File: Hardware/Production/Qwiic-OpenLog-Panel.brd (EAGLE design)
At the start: 90.4 x 94.2 mm, 261 parts, among them J1 SMD, J10 PTH, J11 SMD, J12 ISP, J13 SMD, J14 PTH, J15 SMD, J16 ISP, J17 SMD, J18 PTH, J19 SMD, J2 SMD, J20 ISP, J21 SMD, J22 PTH, J23 SMD, J24 ISP, J25 SMD, J26 PTH, J27 SMD, J28 ISP, J29 SMD, J3 PTH, J30 PTH, J31 SMD, J32 ISP, J33 SMD, J34 PTH, J35 SMD, J36 ISP, J4 SMD, J5 ISP, J6 PTH, J7 SMD, J8 ISP, J9 SMD, Q1 16MHZ, Q2 16MHZ, Q3 16MHZ, Q4 16MHZ, Q5 16MHZ, Q6 16MHZ, Q7 16MHZ, Q8 16MHZ, Q9 16MHZ, U1 microSD Socket, U10 ATMEGA328P_TQFP, U11 microSD Socket, U12 ATMEGA328P_TQFP, U13 microSD Socket, U14 ATMEGA328P_TQFP, U15 microSD Socket, U16 ATMEGA328P_TQFP, U17 microSD Socket, U18 ATMEGA328P_TQFP, U2 ATMEGA328P_TQFP, U3 microSD Socket, U4 ATMEGA328P_TQFP, U5 microSD Socket, U6 ATMEGA328P_TQFP, U7 microSD Socket, U8 ATMEGA328P_TQFP, U9 microSD Socket

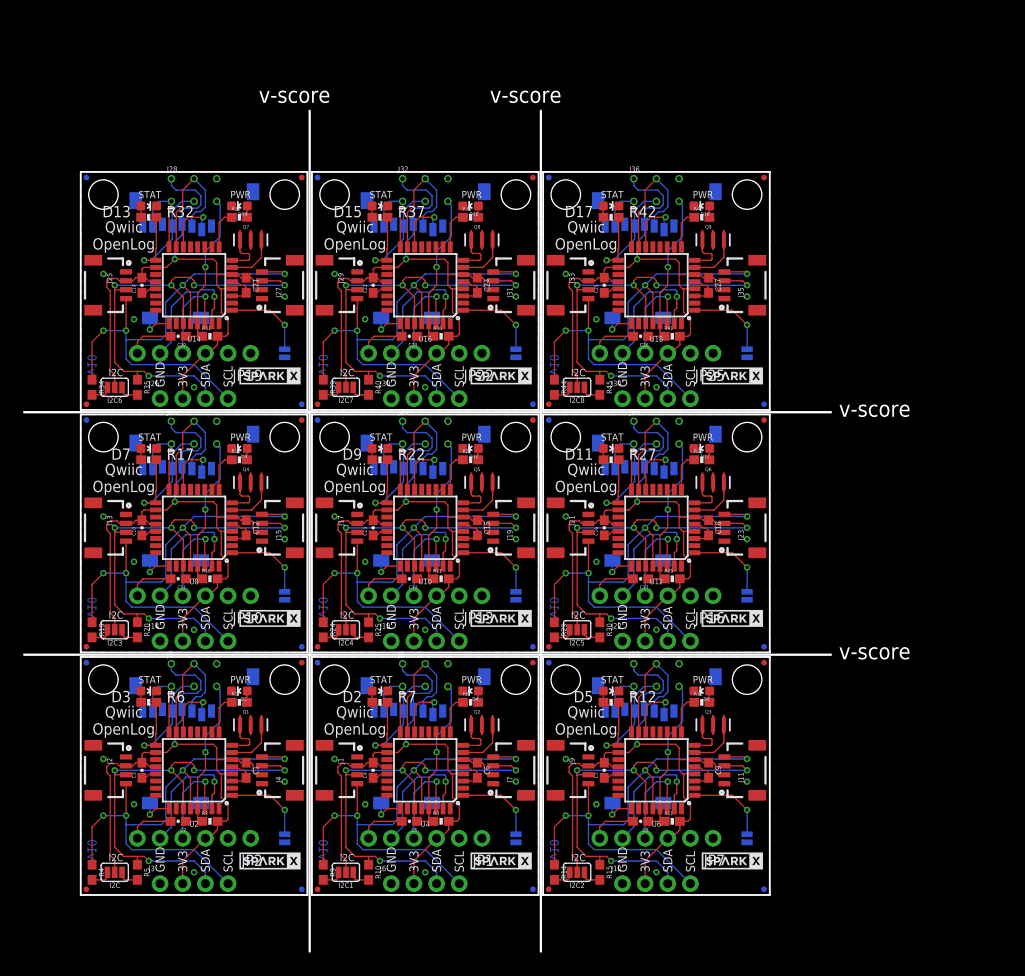
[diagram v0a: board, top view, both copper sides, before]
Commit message: Updating with Buzzard labels
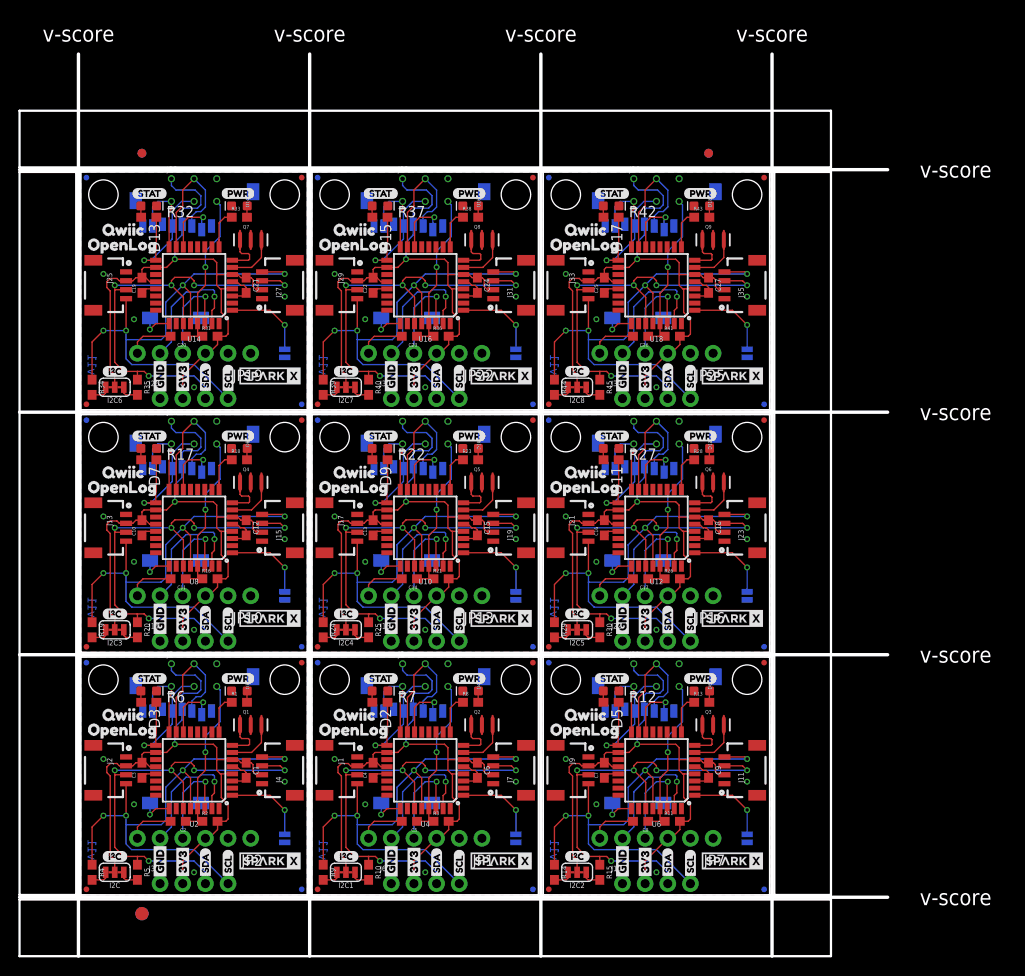
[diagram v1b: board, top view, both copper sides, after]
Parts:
- added E$1, E$2, E$3, E$4: (no value), SparkFun-Aesthetics:FIDUCIAL-1X2
- added E$5, E$6: (no value), SparkFun-Retired:FIDUCIAL-1.5X3
- added U$100, U$119, U$138, U$157, U$24, U$43, U$62, U$81: (no value), Labels:ADR-()-03
- added U$101, U$120, U$139, U$158, U$25, U$44, U$63, U$82: (no value), Labels:I_SUPER2_C-()-03
- added U$102, U$121, U$140, U$159, U$26, U$45, U$64, U$83: (no value), Labels:PWR-()-03
- added U$103, U$122, U$141, U$160, U$27, U$46, U$65, U$84: (no value), buzzard_labels (13):BLK3
- added U$104, U$123, U$142, U$161, U$28, U$47, U$66, U$85: (no value), buzzard_labels (13):BOOT5
- added U$105, U$124, U$143, U$162, U$29, U$48, U$67, U$86: (no value), buzzard_labels (13):GRN4
- added U$106, U$125, U$144, U$163, U$30, U$49, U$68, U$87: (no value), buzzard_labels (13):QWIIC7
- added U$107, U$112, U$126, U$131, U$145, U$150, U$164, U$169, U$19, U$31, U$36, U$50, U$55, U$69, U$74, U$88, U$93: (no value), buzzard_labels (13):SCL2
- added U$108, U$111, U$127, U$130, U$146, U$149, U$165, U$168, U$32, U$35, U$51, U$54, U$70, U$73, U$89, U$92: (no value), buzzard_labels (13):SDA1
- added U$109, U$128, U$147, U$166, U$33, U$52, U$71, U$90: (no value), buzzard_labels (13):STAT0
- added U$110, U$129, U$148, U$167, U$34, U$53, U$72, U$91: (no value), buzzard_labels (14):OPENLOG0
- added U$113, U$132, U$151, U$170, U$37, U$56, U$75, U$94: (no value), buzzard_labels (16):3V30
- added U$114, U$133, U$152, U$171, U$20, U$38, U$57, U$76, U$95: (no value), buzzard_labels (16):GND1
- added U$115, U$134, U$153, U$39, U$58, U$77, U$96: SPARKX-LOGO3, SparkX:SPARKX-SMALL
- added U$116, U$135, U$154, U$21, U$40, U$59, U$78, U$97: SPARKX-LOGO4, SparkX:SPARKX-MEDIUM
- added U$117, U$136, U$155, U$22, U$41, U$60, U$79, U$98: (no value), Labels:3V3-03
- added U$118, U$137, U$156, U$23, U$42, U$61, U$80, U$99: (no value), Labels:GND-03
- C10, C11, C13, C14, C16, C17, C19, C2, C20, C22, C23, C25, C26, C3, C4, C5, C7, C8: device SparkFun-Capacitors:0603-CAP -> SparkFun-Capacitors:0603
- FID1, FID10, FID11, FID12, FID13, FID14, FID15, FID16, FID17, FID18, FID19, FID2, FID20, FID21, FID22, FID23, FID24, FID25, FID26, FID27, FID28, FID29, FID3, FID30, FID31, FID32, FID33, FID34, FID35, FID36, FID4, FID5, FID6, FID7, FID8, FID9: device SparkFun-Aesthetics:MICRO-FIDUCIAL -> SparkFun-Aesthetics:FIDUCIAL-MICRO
- I2C, I2C1, I2C2, I2C3, I2C4, I2C5, I2C6, I2C7, I2C8: value (none) -> JUMPER-SMT_3_2-NC_TRACE_SILK; device SparkFun-Jumpers:SMT-JUMPER_3_2-NC_PASTE_SILK -> SparkFun-Jumpers:SMT-JUMPER_3_2-NC_TRACE_SILK
- J1, J11, J13, J15, J17, J19, J2, J21, J23, J25, J27, J29, J31, J33, J35, J4, J7, J9: device SparkX:1X04_1MM_RA -> SparkFun-Connectors:1X04_1MM_RA
- R1, R13, R18, R23, R28, R33, R38, R43, R8: value 1K -> 1k; device SparkFun-Resistors:0603-RES -> SparkFun-Resistors:0603
- R11, R16, R2, R21, R26, R3, R31, R36, R41: value 10K -> 10k; device SparkFun-Resistors:0603-RES -> SparkFun-Resistors:0603
- R12, R17, R22, R27, R32, R37, R42, R6, R7: device SparkFun-Resistors:0603-RES -> SparkFun-Resistors:0603
- U$10: value SPARKX-LOGO4 -> (none); device SparkX:SPARKX-MEDIUM -> buzzard_labels (13):BLK3
- U$11: value SPARKX-LOGO3 -> (none); device SparkX:SPARKX-SMALL -> buzzard_labels (13):BOOT5
- U$12: value SPARKX-LOGO4 -> (none); device SparkX:SPARKX-MEDIUM -> buzzard_labels (13):GRN4
- U$13: value SPARKX-LOGO3 -> (none); device SparkX:SPARKX-SMALL -> buzzard_labels (13):SDA1
- U$14: value SPARKX-LOGO4 -> (none); device SparkX:SPARKX-MEDIUM -> buzzard_labels (13):QWIIC7
- U$15: value SPARKX-LOGO3 -> (none); device SparkX:SPARKX-SMALL -> buzzard_labels (13):SCL2
- U$16: value SPARKX-LOGO4 -> (none); device SparkX:SPARKX-MEDIUM -> buzzard_labels (13):SDA1
- U$17: value SPARKX-LOGO3 -> (none); device SparkX:SPARKX-SMALL -> buzzard_labels (13):STAT0
- U$18: value SPARKX-LOGO4 -> (none); device SparkX:SPARKX-MEDIUM -> buzzard_labels (14):OPENLOG0
- U$4: value SPARKX-LOGO4 -> (none); device SparkX:SPARKX-MEDIUM -> Labels:3V3-03
- U$5: value SPARKX-LOGO3 -> (none); device SparkX:SPARKX-SMALL -> Labels:GND-03
- U$6: value SPARKX-LOGO4 -> (none); device SparkX:SPARKX-MEDIUM -> buzzard_labels (16):3V30
- U$7: value SPARKX-LOGO3 -> (none); device SparkX:SPARKX-SMALL -> Labels:ADR-()-03
- U$8: value SPARKX-LOGO4 -> (none); device SparkX:SPARKX-MEDIUM -> Labels:I_SUPER2_C-()-03
- U$9: value SPARKX-LOGO3 -> (none); device SparkX:SPARKX-SMALL -> Labels:PWR-()-03
- U10, U12, U14, U16, U18, U2, U4, U6, U8: value ATMEGA328P_TQFP -> ATMEGA328P
- moved U$17 75.4 mm to (5.71, 24.3)
- moved U$18 74.0 mm to (-0.38, 18.5), flipped to the top, turned to 0 degrees
- moved U$11 73.7 mm to (4.32, 4.19), flipped to the bottom, turned to 90 degrees
- moved U$16 68.1 mm to (14.0, 1.78), flipped to the top, turned to 90 degrees
- moved U$5 64.2 mm to (8.89, 1.65), turned to 90 degrees
- moved U$15 64.2 mm to (16.5, 1.78), flipped to the bottom, turned to 90 degrees
- moved U$13 56.9 mm to (14.0, 1.78), flipped to the bottom, turned to 90 degrees
- moved U$12 56.7 mm to (8.13, 8.26), turned to 0 degrees
- moved U$14 48.1 mm to (1.27, 20.2), flipped to the top, turned to 0 degrees
- moved U$6 44.7 mm to (11.4, 1.65), turned to 90 degrees
- moved U$8 36.8 mm to (2.41, 4.32), flipped to the top, turned to 0 degrees
- moved U$10 33.8 mm to (20.7, 8.26), turned to 0 degrees
- moved U$9 32.1 mm to (15.7, 24.3)
- moved U$7 23.0 mm to (24.6, 8.26), flipped to the bottom
- moved U$4 21.0 mm to (11.4, 1.65), flipped to the top, turned to 90 degrees
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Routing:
- net GND6: track 4.65 -> 6.27 mm
- net GND3: track 4.65 -> 6.27 mm
- net GND: track 4.65 -> 6.27 mm
- net GND7: track 4.65 -> 6.27 mm
- net GND4: track 4.65 -> 6.27 mm
- net GND1: track 4.65 -> 6.27 mm
- net GND5: track 4.65 -> 6.27 mm
- net GND2: track 4.65 -> 6.27 mm
- net GND8: track 4.65 -> 6.27 mm
- net N$51: track 4.01 -> 5.03 mm
- net N$59: track 4.67 -> 5.69 mm
- net N$58: track 4.01 -> 5.03 mm
- net N$52: track 4.67 -> 5.69 mm
- net N$45: track 4.67 -> 5.69 mm
- net N$44: track 4.01 -> 5.03 mm
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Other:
- board size 90.4 x 94.2 mm -> 97.3 x 101.1 mm
- board text added: "Qwiic"
- board text added: "v11"
- board text removed: "3V3"
- board text removed: "ADR"
- board text removed: "BLK"
- board text removed: "BOOT"
- board text removed: "GND"
- board text removed: "GRN"
- board text removed: "I2C"
- board text removed: "PWR"
- board text removed: "Qwiic OpenLog"
- board text removed: "SCL"
- board text removed: "SDA"
- board text removed: "STAT"
- board text removed: "v10"

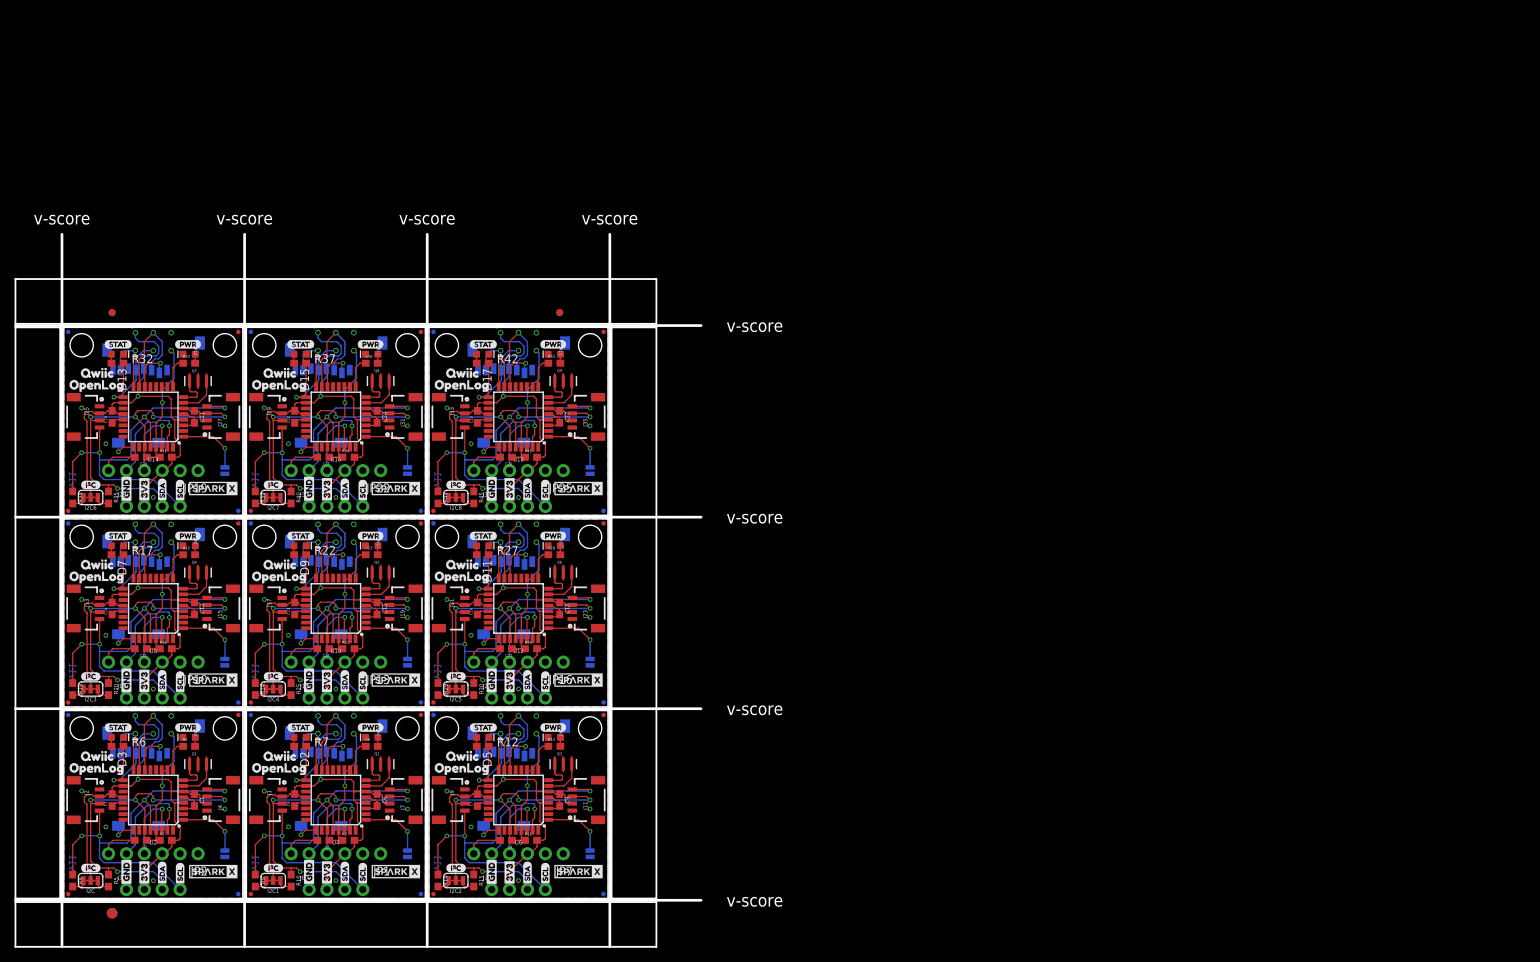
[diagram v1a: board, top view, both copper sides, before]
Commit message: Add v12 production panel
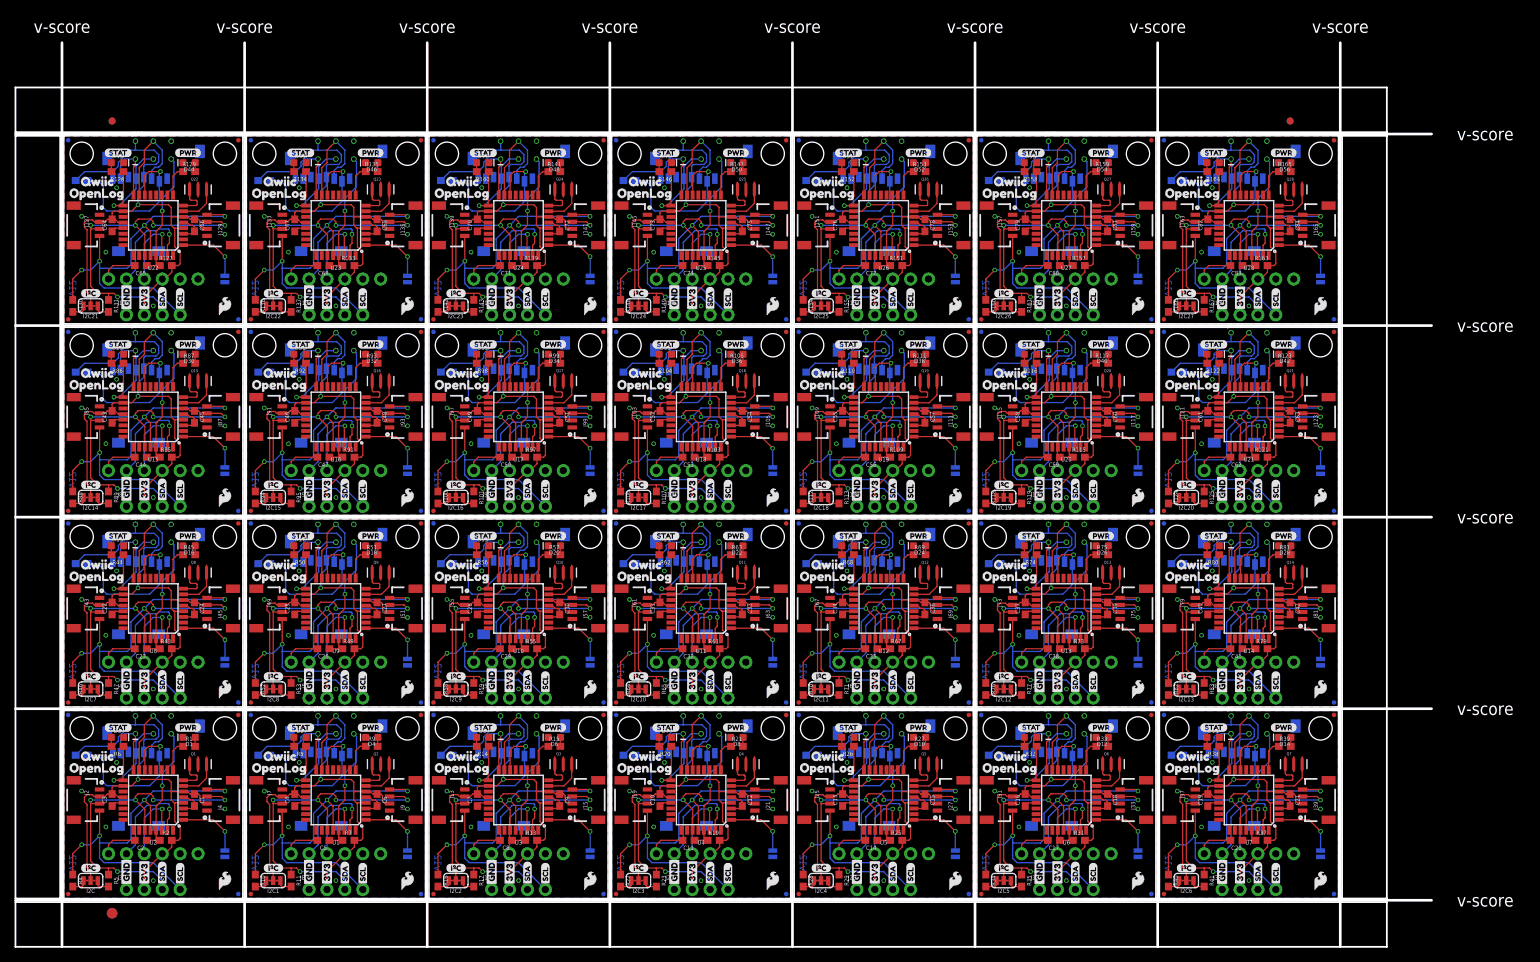
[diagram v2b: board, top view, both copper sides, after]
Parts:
- added ADR10, ADR11, ADR12, ADR13, ADR14, ADR15, ADR16, ADR17, ADR18, ADR19, ADR20, ADR21, ADR22, ADR23, ADR24, ADR25, ADR26, ADR27, ADR9: (no value), SparkFun:SJ_2S-NO
- added C28, C29, C31, C32, C34, C35, C37, C38, C40, C41, C43, C44, C46, C47, C49, C50, C52, C53, C55, C56, C58, C59, C61, C62, C64, C65, C67, C68, C70, C71, C73, C74, C76, C77, C79, C80, C82, C83: 0.1uF, SparkFun-Capacitors:0603
- added C30, C33, C36, C39, C42, C45, C48, C51, C54, C57, C60, C63, C66, C69, C72, C75, C78, C81, C84: 4.7uF, SparkFun-Capacitors:0603
- added D19, D21, D23, D25, D27, D29, D31, D33, D35, D37, D39, D41, D43, D45, D47, D49, D51, D53, D55: GREEN, SparkFun-LED:LED-0603
- added D20, D22, D24, D26, D28, D30, D32, D34, D36, D38, D40, D42, D44, D46, D48, D50, D52, D54, D56: RED, SparkFun-LED:LED-0603
- added FID100, FID101, FID102, FID103, FID104, FID105, FID106, FID107, FID108, FID109, FID110, FID111, FID112, FID37, FID38, FID39, FID40, FID41, FID42, FID43, FID44, FID45, FID46, FID47, FID48, FID49, FID50, FID51, FID52, FID53, FID54, FID55, FID56, FID57, FID58, FID59, FID60, FID61, FID62, FID63, FID64, FID65, FID66, FID67, FID68, FID69, FID70, FID71, FID72, FID73, FID74, FID75, FID76, FID77, FID78, FID79, FID80, FID81, FID82, FID83, FID84, FID85, FID86, FID87, FID88, FID89, FID90, FID91, FID92, FID93, FID94, FID95, FID96, FID97, FID98, FID99: FIDUCIALUFIDUCIAL, SparkFun-Aesthetics:FIDUCIAL-MICRO
- added I2C10, I2C11, I2C12, I2C13, I2C14, I2C15, I2C16, I2C17, I2C18, I2C19, I2C20, I2C21, I2C22, I2C23, I2C24, I2C25, I2C26, I2C27, I2C9: (no value), SparkFun-Jumpers:SMT-JUMPER_3_2-NC_TRACE_SILK
- added J100, J106, J112, J118, J124, J130, J136, J142, J148, J154, J160, J166, J40, J46, J52, J58, J64, J70, J76, J82, J88, J94: ISP, SparkFun-Connectors:2X3_TEST_POINTS
- added J101, J107, J113, J119, J125, J131, J137, J143, J149, J155, J161, J167, J41, J47, J53, J59, J65, J71, J77, J83, J89, J95: (no value), SparkFun-Connectors:1X06_NO_SILK
- added J102, J108, J114, J120, J126, J132, J138, J144, J150, J156, J162, J168, J42, J48, J54, J60, J66, J72, J78, J84, J90, J96: MICRO-SD, SparkFun-Connectors:MICRO-SD-SOCKET
- added J103, J105, J109, J111, J115, J117, J121, J123, J127, J129, J133, J135, J139, J141, J145, J147, J151, J153, J157, J159, J163, J165, J37, J39, J43, J45, J49, J51, J55, J57, J61, J63, J67, J69, J73, J75, J79, J81, J85, J87, J91, J93, J97, J99: SMD, SparkFun-Connectors:1X04_1MM_RA
- added J104, J110, J116, J122, J128, J134, J140, J146, J152, J158, J164, J38, J44, J50, J56, J62, J68, J74, J80, J86, J92, J98: PTH, SparkX:1X04_NO_SILK
- added JP28, JP29, JP30, JP31, JP32, JP33, JP34, JP35, JP36, JP37, JP38, JP39, JP40, JP41, JP42, JP43, JP44, JP45, JP46, JP47, JP48, JP49, JP50, JP51, JP52, JP53, JP54, JP55, JP56: STAND-OFF, SparkFun:STAND-OFF
- added LOGO10, LOGO13, LOGO16, LOGO19, LOGO22, LOGO25, LOGO28, LOGO31, LOGO34, LOGO37, LOGO40, LOGO43, LOGO46, LOGO49, LOGO52, LOGO55, LOGO58, LOGO61, LOGO64, LOGO67, LOGO70, LOGO73, LOGO76, LOGO79, LOGO82: OSHW-LOGOMINI, SparkFun-Aesthetics:OSHW-LOGO-MINI
- added LOGO11, LOGO14, LOGO17, LOGO20, LOGO23, LOGO26, LOGO29, LOGO32, LOGO35, LOGO38, LOGO41, LOGO44, LOGO47, LOGO50, LOGO53, LOGO56, LOGO59, LOGO62, LOGO65, LOGO68, LOGO71, LOGO74, LOGO77, LOGO80, LOGO83: SFE_LOGO_NAME_FLAME.1_INCH, SparkFun-Aesthetics:SFE_LOGO_NAME_FLAME_.1
- added LOGO12, LOGO15, LOGO18, LOGO21, LOGO24, LOGO27, LOGO30, LOGO33, LOGO36, LOGO39, LOGO42, LOGO45, LOGO48, LOGO51, LOGO54, LOGO57, LOGO60, LOGO63, LOGO66, LOGO69, LOGO72, LOGO75, LOGO78, LOGO81, LOGO84: SFE_LOGO_FLAME.1_INCH, SparkFun-Aesthetics:SFE_LOGO_FLAME_.1
- added Q10, Q11, Q12, Q13, Q14, Q15, Q16, Q17, Q18, Q19, Q20, Q21, Q22, Q23, Q24, Q25, Q26, Q27, Q28: 16MHZ, SparkFun-FreqCtrl:RESONATOR-SMD
- added R100, R101, R106, R107, R112, R113, R118, R119, R124, R125, R130, R131, R136, R137, R142, R143, R148, R149, R154, R155, R160, R161, R166, R167, R46, R47, R52, R53, R58, R59, R64, R65, R70, R71, R76, R77, R82, R83, R88, R89, R94, R95: 2.2k, SparkFun-Resistors:0603
- added R102, R103, R108, R109, R114, R115, R120, R121, R126, R127, R132, R133, R138, R139, R144, R145, R150, R151, R156, R157, R162, R163, R168, R48, R49, R54, R55, R60, R61, R66, R67, R72, R73, R78, R79, R84, R85, R90, R91, R96, R97: 10k, SparkFun-Resistors:0603
- added R104, R110, R116, R122, R128, R134, R140, R146, R152, R158, R164, R50, R56, R62, R68, R74, R80, R86, R92, R98: 330, SparkFun-Resistors:0603
- added R105, R111, R117, R123, R129, R135, R141, R147, R153, R159, R165, R51, R57, R63, R69, R75, R81, R87, R93, R99: 1k, SparkFun-Resistors:0603
- added U$172, U$177, U$190, U$195, U$208, U$213, U$226, U$231, U$244, U$249, U$262, U$267, U$280, U$285, U$298, U$303, U$316, U$321, U$334, U$339, U$352, U$357, U$370, U$375, U$388, U$393, U$406, U$411, U$424, U$429, U$442, U$447, U$460, U$465, U$478, U$483, U$496, U$501: (no value), buzzard_labels (13):SCL2
- added U$173, U$176, U$191, U$194, U$209, U$212, U$227, U$230, U$245, U$248, U$263, U$266, U$281, U$284, U$299, U$302, U$317, U$320, U$335, U$338, U$353, U$356, U$371, U$374, U$389, U$392, U$407, U$410, U$425, U$428, U$443, U$446, U$461, U$464, U$479, U$482, U$497, U$500: (no value), buzzard_labels (13):SDA1
- added U$174, U$192, U$210, U$228, U$246, U$264, U$282, U$300, U$318, U$336, U$354, U$372, U$390, U$408, U$426, U$444, U$462, U$480, U$498: (no value), buzzard_labels (13):STAT0
- added U$175, U$193, U$211, U$229, U$247, U$265, U$283, U$301, U$319, U$337, U$355, U$373, U$391, U$409, U$427, U$445, U$463, U$481, U$499: (no value), buzzard_labels (14):OPENLOG0
- added U$178, U$196, U$214, U$232, U$250, U$268, U$286, U$304, U$322, U$340, U$358, U$376, U$394, U$412, U$430, U$448, U$466, U$484, U$502: (no value), buzzard_labels (16):3V30
- added U$179, U$197, U$215, U$233, U$251, U$269, U$287, U$305, U$323, U$341, U$359, U$377, U$395, U$413, U$431, U$449, U$467, U$485, U$503: (no value), buzzard_labels (16):GND1
- added U$180, U$198, U$216, U$234, U$252, U$270, U$288, U$306, U$324, U$342, U$360, U$378, U$396, U$414, U$432, U$450, U$468, U$486, U$504: (no value), Labels:QWIIC-LOGO-SMALL
- added U$181, U$199, U$217, U$235, U$253, U$271, U$289, U$307, U$325, U$343, U$361, U$379, U$397, U$415, U$433, U$451, U$469, U$487: (no value), Labels:3V3-03
- added U$182, U$200, U$218, U$236, U$254, U$272, U$290, U$308, U$326, U$344, U$362, U$380, U$398, U$416, U$434, U$452, U$470, U$488: (no value), Labels:GND-03
- added U$183, U$201, U$219, U$237, U$255, U$273, U$291, U$309, U$327, U$345, U$363, U$381, U$399, U$417, U$435, U$453, U$471, U$489: (no value), Labels:ADR-()-03
- added U$184, U$202, U$220, U$238, U$256, U$274, U$292, U$310, U$328, U$346, U$364, U$382, U$400, U$418, U$436, U$454, U$472, U$490: (no value), Labels:I_SUPER2_C-()-03
- added U$185, U$203, U$221, U$239, U$257, U$275, U$293, U$311, U$329, U$347, U$365, U$383, U$401, U$419, U$437, U$455, U$473, U$491: (no value), Labels:PWR-()-03
- added U$186, U$204, U$222, U$240, U$258, U$276, U$294, U$312, U$330, U$348, U$366, U$384, U$402, U$420, U$438, U$456, U$474, U$492: (no value), buzzard_labels (13):BLK3
- added U$187, U$205, U$223, U$241, U$259, U$277, U$295, U$313, U$331, U$349, U$367, U$385, U$403, U$421, U$439, U$457, U$475, U$493: (no value), buzzard_labels (13):BOOT5
- added U$188, U$206, U$224, U$242, U$260, U$278, U$296, U$314, U$332, U$350, U$368, U$386, U$404, U$422, U$440, U$458, U$476, U$494: (no value), buzzard_labels (13):GRN4
- added U$189, U$207, U$225, U$243, U$261, U$279, U$297, U$315, U$333, U$351, U$369, U$387, U$405, U$423, U$441, U$459, U$477, U$495: (no value), buzzard_labels (13):QWIIC7
- added U19, U20, U21, U22, U23, U24, U25, U26, U27, U28: ATMEGA328P, SparkFun-IC-Microcontroller:TQFP32-08
- I2C, I2C1, I2C2, I2C3, I2C4, I2C5, I2C6, I2C7, I2C8: value JUMPER-SMT_3_2-NC_TRACE_SILK -> (none)
- J1: value SMD -> MICRO-SD; device SparkFun-Connectors:1X04_1MM_RA -> SparkFun-Connectors:MICRO-SD-SOCKET
- J10, J22, J34: value PTH -> ISP; device SparkX:1X04_NO_SILK -> SparkFun-Connectors:2X3_TEST_POINTS
- J11, J17, J23, J29, J35: value SMD -> (none); device SparkFun-Connectors:1X04_1MM_RA -> SparkFun-Connectors:1X06_NO_SILK
- J12, J24, J36: value ISP -> MICRO-SD; device SparkFun-Connectors:2X3_TEST_POINTS -> SparkFun-Connectors:MICRO-SD-SOCKET
- J18, J30: value PTH -> MICRO-SD; device SparkX:1X04_NO_SILK -> SparkFun-Connectors:MICRO-SD-SOCKET
- J20, J32, J8: value ISP -> PTH; device SparkFun-Connectors:2X3_TEST_POINTS -> SparkX:1X04_NO_SILK
- J6: value PTH -> (none); device SparkX:1X04_NO_SILK -> SparkFun-Connectors:1X06_NO_SILK
- JP1, JP10, JP13, JP16, JP19, JP2, JP22, JP25, JP7: value BOOT -> STAND-OFF; device SparkFun-Connectors:1X06_NO_SILK -> SparkFun:STAND-OFF
- LOGO1, LOGO6, LOGO9: value OSHW-LOGOMINI -> SFE_LOGO_FLAME.1_INCH; device SparkFun-Aesthetics:OSHW-LOGO-MINI -> SparkFun-Aesthetics:SFE_LOGO_FLAME_.1
- LOGO4, LOGO5, LOGO8: value OSHW-LOGOMINI -> SFE_LOGO_NAME_FLAME.1_INCH; device SparkFun-Aesthetics:OSHW-LOGO-MINI -> SparkFun-Aesthetics:SFE_LOGO_NAME_FLAME_.1
- R11, R16, R41: value 10k -> 2.2k
- R12, R37, R42, R7: value 330 -> 10k
- R13, R18, R43: value 1k -> 10k
- R14, R20, R44: value 2.2k -> 330
- R15, R39, R45, R9: value 2.2k -> 1k
- R17, R22: value 330 -> 2.2k
- R19, R24, R25, R30: value 2.2k -> 10k
- R21: value 10k -> 1k
- R23, R28: value 1k -> 2.2k
- R26: value 10k -> 330
- R27: value 330 -> 1k
- R38, R8: value 1k -> 330
- U$1: value SPARKX-LOGO4 -> (none); device SparkX:SPARKX-MEDIUM -> Labels:3V3-03
- U$100: device Labels:ADR-()-03 -> buzzard_labels (13):SCL2
- U$101, U$158: device Labels:I_SUPER2_C-()-03 -> buzzard_labels (13):SDA1
- U$102: device Labels:PWR-()-03 -> buzzard_labels (13):STAT0
- U$103: device buzzard_labels (13):BLK3 -> buzzard_labels (14):OPENLOG0
- U$104, U$47: device buzzard_labels (13):BOOT5 -> buzzard_labels (13):SDA1
- U$105: device buzzard_labels (13):GRN4 -> buzzard_labels (13):SCL2
- U$106: device buzzard_labels (13):QWIIC7 -> buzzard_labels (16):3V30
- U$107: device buzzard_labels (13):SCL2 -> buzzard_labels (16):GND1
- U$108, U$54: device buzzard_labels (13):SDA1 -> Labels:QWIIC-LOGO-SMALL
- U$109: device buzzard_labels (13):STAT0 -> Labels:3V3-03
- U$110: device buzzard_labels (14):OPENLOG0 -> Labels:GND-03
- U$111, U$165: device buzzard_labels (13):SDA1 -> Labels:ADR-()-03
- U$112: device buzzard_labels (13):SCL2 -> Labels:I_SUPER2_C-()-03
- U$113: device buzzard_labels (16):3V30 -> Labels:PWR-()-03
- U$114: device buzzard_labels (16):GND1 -> buzzard_labels (13):BLK3
- U$115: value SPARKX-LOGO3 -> (none); device SparkX:SPARKX-SMALL -> buzzard_labels (13):BOOT5
- U$116: value SPARKX-LOGO4 -> (none); device SparkX:SPARKX-MEDIUM -> buzzard_labels (13):GRN4
- U$117: device Labels:3V3-03 -> buzzard_labels (13):QWIIC7
- U$118: device Labels:GND-03 -> buzzard_labels (13):SCL2
- U$119: device Labels:ADR-()-03 -> buzzard_labels (13):SDA1
- U$120: device Labels:I_SUPER2_C-()-03 -> buzzard_labels (13):STAT0
- U$121: device Labels:PWR-()-03 -> buzzard_labels (14):OPENLOG0
- U$122, U$65: device buzzard_labels (13):BLK3 -> buzzard_labels (13):SDA1
- U$123, U$28: device buzzard_labels (13):BOOT5 -> buzzard_labels (13):SCL2
- U$124: device buzzard_labels (13):GRN4 -> buzzard_labels (16):3V30
- U$125: device buzzard_labels (13):QWIIC7 -> buzzard_labels (16):GND1
- U$126, U$36: device buzzard_labels (13):SCL2 -> Labels:QWIIC-LOGO-SMALL
- U$127, U$73: device buzzard_labels (13):SDA1 -> Labels:3V3-03
- U$128: device buzzard_labels (13):STAT0 -> Labels:GND-03
- U$129: device buzzard_labels (14):OPENLOG0 -> Labels:ADR-()-03
- U$130: device buzzard_labels (13):SDA1 -> Labels:I_SUPER2_C-()-03
- U$131: device buzzard_labels (13):SCL2 -> Labels:PWR-()-03
- U$132: device buzzard_labels (16):3V30 -> buzzard_labels (13):BLK3
- U$133: device buzzard_labels (16):GND1 -> buzzard_labels (13):BOOT5
- U$134: value SPARKX-LOGO3 -> (none); device SparkX:SPARKX-SMALL -> buzzard_labels (13):GRN4
- U$135: value SPARKX-LOGO4 -> (none); device SparkX:SPARKX-MEDIUM -> buzzard_labels (13):QWIIC7
- U$136: device Labels:3V3-03 -> buzzard_labels (13):SCL2
- U$137: device Labels:GND-03 -> buzzard_labels (13):SDA1
- U$138: device Labels:ADR-()-03 -> buzzard_labels (13):STAT0
- U$139: device Labels:I_SUPER2_C-()-03 -> buzzard_labels (14):OPENLOG0
- U$140, U$83: device Labels:PWR-()-03 -> buzzard_labels (13):SDA1
- U$141, U$46: device buzzard_labels (13):BLK3 -> buzzard_labels (13):SCL2
- U$142: device buzzard_labels (13):BOOT5 -> buzzard_labels (16):3V30
- U$143: device buzzard_labels (13):GRN4 -> buzzard_labels (16):GND1
- U$144: device buzzard_labels (13):QWIIC7 -> Labels:QWIIC-LOGO-SMALL
- U$145, U$55: device buzzard_labels (13):SCL2 -> Labels:3V3-03
- U$146, U$92: device buzzard_labels (13):SDA1 -> Labels:GND-03
- U$147: device buzzard_labels (13):STAT0 -> Labels:ADR-()-03
- U$148: device buzzard_labels (14):OPENLOG0 -> Labels:I_SUPER2_C-()-03
- U$149: device buzzard_labels (13):SDA1 -> Labels:PWR-()-03
- U$150: device buzzard_labels (13):SCL2 -> buzzard_labels (13):BLK3
- U$151: device buzzard_labels (16):3V30 -> buzzard_labels (13):BOOT5
- U$152: device buzzard_labels (16):GND1 -> buzzard_labels (13):GRN4
- U$153: value SPARKX-LOGO3 -> (none); device SparkX:SPARKX-SMALL -> buzzard_labels (13):QWIIC7
- U$154: value SPARKX-LOGO4 -> (none); device SparkX:SPARKX-MEDIUM -> buzzard_labels (13):SCL2
- U$155: device Labels:3V3-03 -> buzzard_labels (13):SDA1
- U$156: device Labels:GND-03 -> buzzard_labels (13):STAT0
- U$157: device Labels:ADR-()-03 -> buzzard_labels (14):OPENLOG0
- U$159, U$64: device Labels:PWR-()-03 -> buzzard_labels (13):SCL2
- U$160: device buzzard_labels (13):BLK3 -> buzzard_labels (16):3V30
- U$161: device buzzard_labels (13):BOOT5 -> buzzard_labels (16):GND1
- U$162: device buzzard_labels (13):GRN4 -> Labels:QWIIC-LOGO-SMALL
- U$163: device buzzard_labels (13):QWIIC7 -> Labels:3V3-03
- U$164, U$74: device buzzard_labels (13):SCL2 -> Labels:GND-03
- U$166: device buzzard_labels (13):STAT0 -> Labels:I_SUPER2_C-()-03
- U$167: device buzzard_labels (14):OPENLOG0 -> Labels:PWR-()-03
- U$168: device buzzard_labels (13):SDA1 -> buzzard_labels (13):BLK3
- U$169: device buzzard_labels (13):SCL2 -> buzzard_labels (13):BOOT5
- U$170: device buzzard_labels (16):3V30 -> buzzard_labels (13):GRN4
- U$171: device buzzard_labels (16):GND1 -> buzzard_labels (13):QWIIC7
- U$2: value SPARKX-LOGO3 -> (none); device SparkX:SPARKX-SMALL -> Labels:GND-03
- U$21: value SPARKX-LOGO4 -> (none); device SparkX:SPARKX-MEDIUM -> Labels:ADR-()-03
- U$22: device Labels:3V3-03 -> Labels:I_SUPER2_C-()-03
- U$23: device Labels:GND-03 -> Labels:PWR-()-03
- U$24: device Labels:ADR-()-03 -> buzzard_labels (13):BLK3
- U$25: device Labels:I_SUPER2_C-()-03 -> buzzard_labels (13):BOOT5
- U$26: device Labels:PWR-()-03 -> buzzard_labels (13):GRN4
- U$27: device buzzard_labels (13):BLK3 -> buzzard_labels (13):QWIIC7
- U$29, U$86: device buzzard_labels (13):GRN4 -> buzzard_labels (13):SDA1
- U$3: value SPARKX-LOGO3 -> (none); device SparkX:SPARKX-SMALL -> Labels:QWIIC-LOGO-SMALL
- U$30: device buzzard_labels (13):QWIIC7 -> buzzard_labels (13):STAT0
- U$31: device buzzard_labels (13):SCL2 -> buzzard_labels (14):OPENLOG0
- U$33: device buzzard_labels (13):STAT0 -> buzzard_labels (13):SCL2
- U$34: device buzzard_labels (14):OPENLOG0 -> buzzard_labels (16):3V30
- U$35, U$89: device buzzard_labels (13):SDA1 -> buzzard_labels (16):GND1
- U$37: device buzzard_labels (16):3V30 -> Labels:3V3-03
- U$38: device buzzard_labels (16):GND1 -> Labels:GND-03
- U$39: value SPARKX-LOGO3 -> (none); device SparkX:SPARKX-SMALL -> Labels:ADR-()-03
- U$40: value SPARKX-LOGO4 -> (none); device SparkX:SPARKX-MEDIUM -> Labels:I_SUPER2_C-()-03
- U$41: device Labels:3V3-03 -> Labels:PWR-()-03
- U$42: device Labels:GND-03 -> buzzard_labels (13):BLK3
- U$43: device Labels:ADR-()-03 -> buzzard_labels (13):BOOT5
- U$44: device Labels:I_SUPER2_C-()-03 -> buzzard_labels (13):GRN4
- U$45: device Labels:PWR-()-03 -> buzzard_labels (13):QWIIC7
- U$48: device buzzard_labels (13):GRN4 -> buzzard_labels (13):STAT0
- U$49: device buzzard_labels (13):QWIIC7 -> buzzard_labels (14):OPENLOG0
- U$50: device buzzard_labels (13):SCL2 -> buzzard_labels (13):SDA1
- U$51: device buzzard_labels (13):SDA1 -> buzzard_labels (13):SCL2
- U$52: device buzzard_labels (13):STAT0 -> buzzard_labels (16):3V30
- U$53: device buzzard_labels (14):OPENLOG0 -> buzzard_labels (16):GND1
- U$56: device buzzard_labels (16):3V30 -> Labels:GND-03
- U$57: device buzzard_labels (16):GND1 -> Labels:ADR-()-03
- U$58: value SPARKX-LOGO3 -> (none); device SparkX:SPARKX-SMALL -> Labels:I_SUPER2_C-()-03
- U$59: value SPARKX-LOGO4 -> (none); device SparkX:SPARKX-MEDIUM -> Labels:PWR-()-03
- U$60: device Labels:3V3-03 -> buzzard_labels (13):BLK3
- U$61: device Labels:GND-03 -> buzzard_labels (13):BOOT5
- U$62: device Labels:ADR-()-03 -> buzzard_labels (13):GRN4
- U$63: device Labels:I_SUPER2_C-()-03 -> buzzard_labels (13):QWIIC7
- U$66: device buzzard_labels (13):BOOT5 -> buzzard_labels (13):STAT0
- U$67: device buzzard_labels (13):GRN4 -> buzzard_labels (14):OPENLOG0
- U$68: device buzzard_labels (13):QWIIC7 -> buzzard_labels (13):SDA1
- U$70: device buzzard_labels (13):SDA1 -> buzzard_labels (16):3V30
- U$71: device buzzard_labels (13):STAT0 -> buzzard_labels (16):GND1
- U$72: device buzzard_labels (14):OPENLOG0 -> Labels:QWIIC-LOGO-SMALL
- U$75: device buzzard_labels (16):3V30 -> Labels:ADR-()-03
- U$76: device buzzard_labels (16):GND1 -> Labels:I_SUPER2_C-()-03
- U$77: value SPARKX-LOGO3 -> (none); device SparkX:SPARKX-SMALL -> Labels:PWR-()-03
- U$78: value SPARKX-LOGO4 -> (none); device SparkX:SPARKX-MEDIUM -> buzzard_labels (13):BLK3
- U$79: device Labels:3V3-03 -> buzzard_labels (13):BOOT5
- U$80: device Labels:GND-03 -> buzzard_labels (13):GRN4
- U$81: device Labels:ADR-()-03 -> buzzard_labels (13):QWIIC7
- U$82: device Labels:I_SUPER2_C-()-03 -> buzzard_labels (13):SCL2
- U$84: device buzzard_labels (13):BLK3 -> buzzard_labels (13):STAT0
- U$85: device buzzard_labels (13):BOOT5 -> buzzard_labels (14):OPENLOG0
- U$87: device buzzard_labels (13):QWIIC7 -> buzzard_labels (13):SCL2
- U$88: device buzzard_labels (13):SCL2 -> buzzard_labels (16):3V30
- U$90: device buzzard_labels (13):STAT0 -> Labels:QWIIC-LOGO-SMALL
- U$91: device buzzard_labels (14):OPENLOG0 -> Labels:3V3-03
- U$93: device buzzard_labels (13):SCL2 -> Labels:ADR-()-03
- U$94: device buzzard_labels (16):3V30 -> Labels:I_SUPER2_C-()-03
- U$95: device buzzard_labels (16):GND1 -> Labels:PWR-()-03
- U$96: value SPARKX-LOGO3 -> (none); device SparkX:SPARKX-SMALL -> buzzard_labels (13):BLK3
- U$97: value SPARKX-LOGO4 -> (none); device SparkX:SPARKX-MEDIUM -> buzzard_labels (13):BOOT5
- U$98: device Labels:3V3-03 -> buzzard_labels (13):GRN4
- U$99: device Labels:GND-03 -> buzzard_labels (13):QWIIC7
- U1, U11, U13, U15, U17, U3, U5, U7, U9: value microSD Socket -> ATMEGA328P; device SparkFun-Connectors:MICRO-SD-SOCKET-PP -> SparkFun-IC-Microcontroller:TQFP32-08
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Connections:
- removed net CD: U2.25, U3.CD1
- removed net CD1: U1.CD1, U4.25
- removed net CD2: U5.CD1, U6.25
- removed net CD3: U7.CD1, U8.25
- removed net CD4: U10.25, U9.CD1
- removed net CD5: U11.CD1, U12.25
- removed net CD6: U13.CD1, U14.25
- removed net CD7: U15.CD1, U16.25
- removed net CD8: U17.CD1, U18.25
- new net 3.3V10: C31.2, C33.1, I2C10.2, J61.2, J62.2, J63.2, J64.2, J65.3, J66.VCC, R61.2, R66.2, U11.18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
- new net 3.3V11: C34.2, C36.1, I2C11.2, J67.2, J68.2, J69.2, J70.2, J71.3, J72.VCC, R67.2, R72.2, U12.18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
- new net 3.3V12: C37.2, C39.1, I2C12.2, J73.2, J74.2, J75.2, J76.2, J77.3, J78.VCC, R73.2, R78.2, U13.18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
- new net 3.3V13: C40.2, C42.1, I2C13.2, J79.2, J80.2, J81.2, J82.2, J83.3, J84.VCC, R79.2, R84.2, U14.18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
- new net 3.3V14: C43.2, C45.1, I2C14.2, J85.2, J86.2, J87.2, J88.2, J89.3, J90.VCC, R85.2, R90.2, U15.18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
- new net 3.3V15: C46.2, C48.1, I2C15.2, J91.2, J92.2, J93.2, J94.2, J95.3, J96.VCC, R91.2, R96.2, U16.18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
- new net 3.3V16: C49.2, C51.1, I2C16.2, J100.2, J101.3, J102.VCC, J97.2, J98.2, J99.2, R102.2, R97.2, U17.18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
- new net 3.3V17: C52.2, C54.1, I2C17.2, J103.2, J104.2, J105.2, J106.2, J107.3, J108.VCC, R103.2, R108.2, U18.18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
- new net 3.3V18: C55.2, C57.1, I2C18.2, J109.2, J110.2, J111.2, J112.2, J113.3, J114.VCC, R109.2, R114.2, U19.18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
- new net 3.3V19: C58.2, C60.1, I2C19.2, J115.2, J116.2, J117.2, J118.2, J119.3, J120.VCC, R115.2, R120.2, U20.18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
- new net 3.3V20: C61.2, C63.1, I2C20.2, J121.2, J122.2, J123.2, J124.2, J125.3, J126.VCC, R121.2, R126.2, U21.18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
- new net 3.3V21: C64.2, C66.1, I2C21.2, J127.2, J128.2, J129.2, J130.2, J131.3, J132.VCC, R127.2, R132.2, U22.18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
- new net 3.3V22: C67.2, C69.1, I2C22.2, J133.2, J134.2, J135.2, J136.2, J137.3, J138.VCC, R133.2, R138.2, U23.18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
- new net 3.3V23: C70.2, C72.1, I2C23.2, J139.2, J140.2, J141.2, J142.2, J143.3, J144.VCC, R139.2, R144.2, U24.18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
- new net 3.3V24: C73.2, C75.1, I2C24.2, J145.2, J146.2, J147.2, J148.2, J149.3, J150.VCC, R145.2, R150.2, U25.18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
- new net 3.3V25: C76.2, C78.1, I2C25.2, J151.2, J152.2, J153.2, J154.2, J155.3, J156.VCC, R151.2, R156.2, U26.18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
- new net 3.3V26: C79.2, C81.1, I2C26.2, J157.2, J158.2, J159.2, J160.2, J161.3, J162.VCC, R157.2, R162.2, U27.18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
- new net 3.3V27: C82.2, C84.1, I2C27.2, J163.2, J164.2, J165.2, J166.2, J167.3, J168.VCC, R163.2, R168.2, U28.18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
- new net 3.3V9: C28.2, C30.1, I2C9.2, J55.2, J56.2, J57.2, J58.2, J59.3, J60.VCC, R55.2, R60.2, U10.18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
- new net ADDR10: ADR10.2, U11.1
- new net ADDR11: ADR11.2, U12.1
- new net ADDR12: ADR12.2, U13.1
- new net ADDR13: ADR13.2, U14.1
- new net ADDR14: ADR14.2, U15.1
- new net ADDR15: ADR15.2, U16.1
- new net ADDR16: ADR16.2, U17.1
- new net ADDR17: ADR17.2, U18.1
- new net ADDR18: ADR18.2, U19.1
- new net ADDR19: ADR19.2, U20.1
- new net ADDR20: ADR20.2, U21.1
- new net ADDR21: ADR21.2, U22.1
- new net ADDR22: ADR22.2, U23.1
- new net ADDR23: ADR23.2, U24.1
- new net ADDR24: ADR24.2, U25.1
- new net ADDR25: ADR25.2, U26.1
- new net ADDR26: ADR26.2, U27.1
- new net ADDR27: ADR27.2, U28.1
- new net ADDR9: ADR9.2, U10.1
- new net CS10: J66.CS, R66.1, U11.14
- new net CS11: J72.CS, R72.1, U12.14
- new net CS12: J78.CS, R78.1, U13.14
- new net CS13: J84.CS, R84.1, U14.14
- new net CS14: J90.CS, R90.1, U15.14
- new net CS15: J96.CS, R96.1, U16.14
- new net CS16: J102.CS, R102.1, U17.14
- new net CS17: J108.CS, R108.1, U18.14
- new net CS18: J114.CS, R114.1, U19.14
- new net CS19: J120.CS, R120.1, U20.14
- new net CS20: J126.CS, R126.1, U21.14
- new net CS21: J132.CS, R132.1, U22.14
- new net CS22: J138.CS, R138.1, U23.14
- new net CS23: J144.CS, R144.1, U24.14
- new net CS24: J150.CS, R150.1, U25.14
- new net CS25: J156.CS, R156.1, U26.14
- new net CS26: J162.CS, R162.1, U27.14
- new net CS27: J168.CS, R168.1, U28.14
- new net CS9: J60.CS, R60.1, U10.14
- new net DTR10: C32.2, J65.6
- new net DTR11: C35.2, J71.6
- new net DTR12: C38.2, J77.6
- new net DTR13: C41.2, J83.6
- new net DTR14: C44.2, J89.6
- new net DTR15: C47.2, J95.6
- new net DTR16: C50.2, J101.6
- new net DTR17: C53.2, J107.6
- new net DTR18: C56.2, J113.6
- new net DTR19: C59.2, J119.6
- new net DTR20: C62.2, J125.6
- new net DTR21: C65.2, J131.6
- new net DTR22: C68.2, J137.6
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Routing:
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- added copper zone on layer 1, net GND10
- added copper zone on layer 16, net GND10
- added copper zone on layer 1, net GND11
- added copper zone on layer 16, net GND11
- added copper zone on layer 1, net GND12
- added copper zone on layer 16, net GND12
- added copper zone on layer 1, net GND13
- added copper zone on layer 16, net GND13
- added copper zone on layer 1, net GND14
- added copper zone on layer 16, net GND14
- added copper zone on layer 1, net GND15
- added copper zone on layer 16, net GND15
- added copper zone on layer 1, net GND16
- added copper zone on layer 16, net GND16
- added copper zone on layer 1, net GND17
- added copper zone on layer 16, net GND17
- added copper zone on layer 1, net GND18
- added copper zone on layer 16, net GND18
- added copper zone on layer 1, net GND19
- added copper zone on layer 16, net GND19
- added copper zone on layer 1, net GND20
- added copper zone on layer 16, net GND20
- added copper zone on layer 1, net GND21
- added copper zone on layer 16, net GND21
- added copper zone on layer 1, net GND22
- added copper zone on layer 16, net GND22
- added copper zone on layer 1, net GND23
- added copper zone on layer 16, net GND23
- added copper zone on layer 1, net GND24
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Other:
- board size 97.3 x 101.1 mm -> 200.9 x 128.3 mm
- board text added: "v12"
- board text removed: "v11"
